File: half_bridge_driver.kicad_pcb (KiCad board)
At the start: 2 copper layers, 20 x 6 mm, 7 parts, among them J1 Conn_01x01_Male, J2 Conn_01x01_Male, U1 ZXGD3003E6, U2 ZXGD3003E6

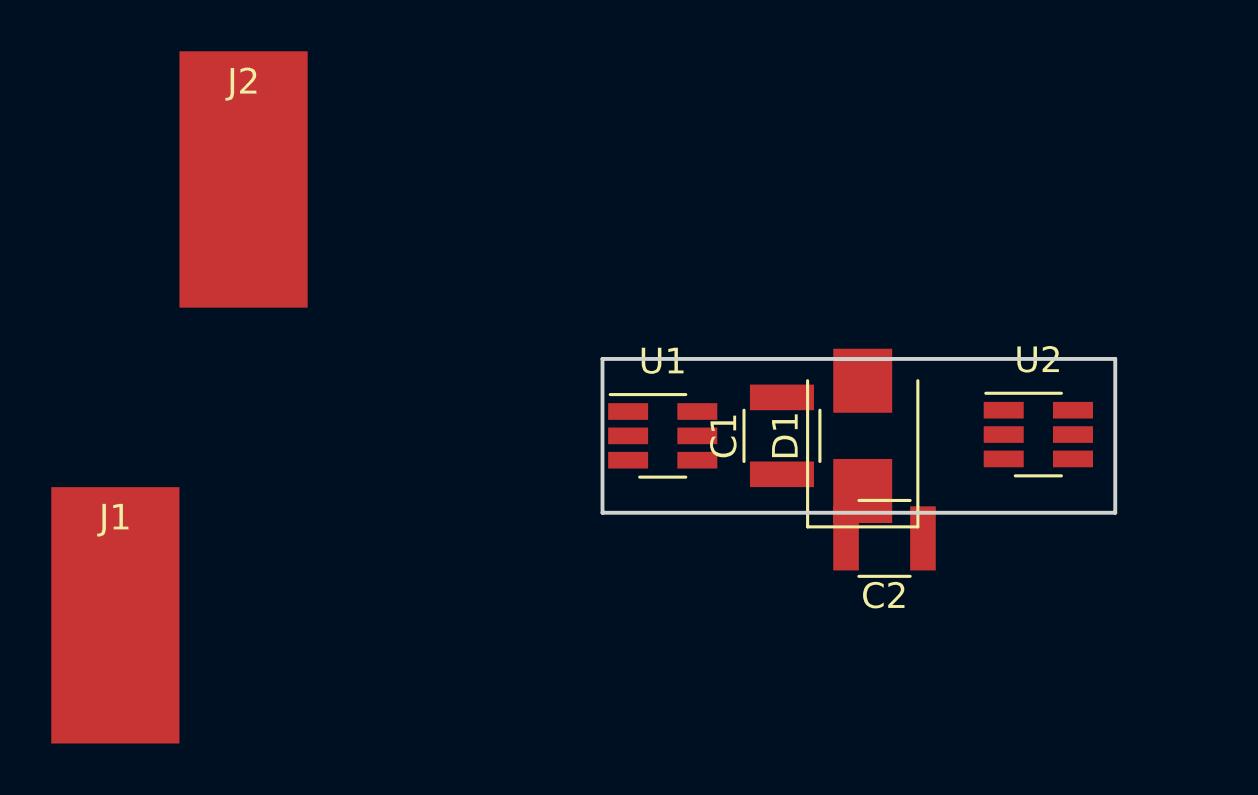
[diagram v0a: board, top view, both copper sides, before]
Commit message: Fixed high driver orientation and added one pad for external wiring.
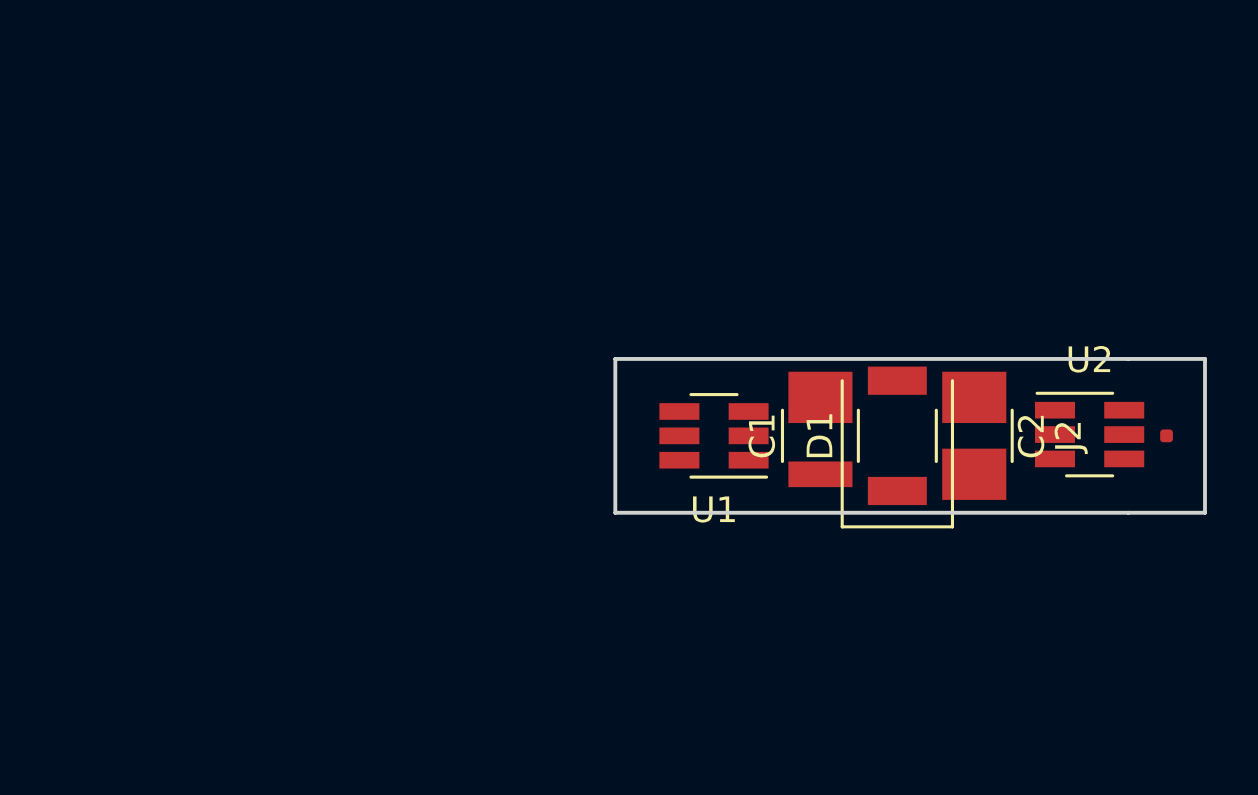
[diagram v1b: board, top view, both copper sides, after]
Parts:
- removed J1: Conn_01x01_Male, Wire_Pads:SolderWirePad_single_SMD_5x10mm
- C1, C2: value C -> 10µF
- D1: value D -> GB01SLT12-214
- moved J2 37.4 mm to (157.0, 90.0), turned to 90 degrees
- moved C2 5.32 mm to (149.5, 90.0), turned to 270 degrees
- moved U1 2.00 mm to (139.3, 90.0), turned to 180 degrees
- moved U2 2.00 mm to (154.0, 90.0)
- moved C1 1.50 mm to (143.5, 90.0)
- moved D1 1.35 mm to (146.5, 90.0)
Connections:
- U1 pad 1: /GND_High_Side -> /15V_High_Side
- U1 pad 3: /15V_High_Side -> /GND_High_Side
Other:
- board size 20 x 6 mm -> 23 x 6 mm
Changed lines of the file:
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@@
   (general
     (thickness 1.6)
-    (drawings 4)
+    (drawings 6)
     (tracks 0)
     (zones 0)
-    (modules 7)
+    (modules 6)
     (nets 9)
   )
@@
     (mod_text_size 1 1)
     (mod_text_width 0.15)
-    (pad_size 1.524 1.524)
-    (pad_drill 0.762)
+    (pad_size 0.5 0.5)
+    (pad_drill 0)
     (pad_to_mask_clearance 0.2)
     (aux_axis_origin 0 0)
@@
   )
   (module Capacitors_SMD:C_1210 (layer F.Cu)
-    (at 142 90 90)
+    (at 143.5 90 90)
     (descr "Capacitor SMD 1210, reflow soldering, AVX (see smccp.pdf)")
     (tags "capacitor 1210")
@@
       (effects (font (size 1 1) (thickness 0.15)))
     )
-    (fp_text value C (at 0 2.5 90) (layer F.Fab)
+    (fp_text value 10µF (at 0 2.5 90) (layer F.Fab)
       (effects (font (size 1 1) (thickness 0.15)))
     )
@@
       (effects (font (size 1 1) (thickness 0.15)))
     )
-    (pad 2 smd rect (at 1.5 0 90) (size 1 2.5) (layers F.Cu F.Paste F.Mask)
+    (pad 2 smd rect (at 1.5 0 90) (size 2 2.5) (layers F.Cu F.Paste F.Mask)
       (net 1 /GND_High_Side))
     (pad 1 smd rect (at -1.5 0 90) (size 1 2.5) (layers F.Cu F.Paste F.Mask)
@@
   )
   (module Capacitors_SMD:C_1210 (layer F.Cu)
-    (at 146 94 180)
+    (at 149.5 90 270)
     (descr "Capacitor SMD 1210, reflow soldering, AVX (see smccp.pdf)")
     (tags "capacitor 1210")
     (attr smd)
-    (fp_text reference C2 (at 0 -2.25 180) (layer F.SilkS)
-      (effects (font (size 1 1) (thickness 0.15)))
-    )
-    (fp_text value C (at 0 2.5 180) (layer F.Fab)
-      (effects (font (size 1 1) (thickness 0.15)))
-    )
-    (fp_text user %R (at 0 -2.25 180) (layer F.Fab)
+    (fp_text reference C2 (at 0 -2.25 270) (layer F.SilkS)
+      (effects (font (size 1 1) (thickness 0.15)))
+    )
+    (fp_text value 10µF (at 0 2.5 270) (layer F.Fab)
+      (effects (font (size 1 1) (thickness 0.15)))
+    )
+    (fp_text user %R (at 0 -2.25 270) (layer F.Fab)
       (effects (font (size 1 1) (thickness 0.15)))
     )
@@
     (fp_line (start 2.25 1.5) (end 2.25 -1.5) (layer F.CrtYd) (width 0.05))
     (fp_line (start 2.25 1.5) (end -2.25 1.5) (layer F.CrtYd) (width 0.05))
-    (pad 1 smd rect (at -1.5 0 180) (size 1 2.5) (layers F.Cu F.Paste F.Mask)
+    (pad 1 smd rect (at -1.5 0 270) (size 2 2.5) (layers F.Cu F.Paste F.Mask)
       (net 3 +15V))
-    (pad 2 smd rect (at 1.5 0 180) (size 1 2.5) (layers F.Cu F.Paste F.Mask)
+    (pad 2 smd rect (at 1.5 0 270) (size 2 2.5) (layers F.Cu F.Paste F.Mask)
       (net 4 GND))
     (model Capacitors_SMD.3dshapes/C_1210.wrl
@@
   )
   (module Diodes_SMD:D_SMB (layer F.Cu)
-    (at 145.15 90 90)
+    (at 146.5 90 90)
     (descr "Diode SMB (DO-214AA)")
     (tags "Diode SMB (DO-214AA)")
@@
       (effects (font (size 1 1) (thickness 0.15)))
     )
-    (fp_text value D (at 0 3.1 90) (layer F.Fab)
+    (fp_text value GB01SLT12-214 (at 0 3.1 90) (layer F.Fab)
       (effects (font (size 1 1) (thickness 0.15)))
     )
@@
       (effects (font (size 1 1) (thickness 0.15)))
     )
-    (pad 2 smd rect (at 2.15 0 90) (size 2.5 2.3) (layers F.Cu F.Paste F.Mask)
+    (pad 2 smd rect (at 2.15 0 90) (size 1.1 2.3) (layers F.Cu F.Paste F.Mask)
       (net 3 +15V))
-    (pad 1 smd rect (at -2.15 0 90) (size 2.5 2.3) (layers F.Cu F.Paste F.Mask)
+    (pad 1 smd rect (at -2.15 0 90) (size 1.1 2.3) (layers F.Cu F.Paste F.Mask)
       (net 1 /GND_High_Side))
     (model ${KISYS3DMOD}/Diodes_SMD.3dshapes/D_SMB.wrl
@@
   )
   (module Wire_Pads:SolderWirePad_single_SMD_5x10mm (layer F.Cu)
-    (at 116 97)
+    (at 157 90 90)
     (descr "Wire Pad, Square, SMD Pad,  5mm x 10mm,")
     (tags "MesurementPoint Square SMDPad 5mmx10mm ")
     (attr smd)
-    (fp_text reference J1 (at 0 -3.81) (layer F.SilkS)
-      (effects (font (size 1 1) (thickness 0.15)))
-    )
-    (fp_text value Conn_01x01_Male (at 0 6.35) (layer F.Fab)
-      (effects (font (size 1 1) (thickness 0.15)))
-    )
-    (fp_line (start -2.75 -5.25) (end -2.75 5.25) (layer F.CrtYd) (width 0.05))
-    (fp_line (start -2.75 5.25) (end 2.75 5.25) (layer F.CrtYd) (width 0.05))
-    (fp_line (start 2.75 5.25) (end 2.75 -5.25) (layer F.CrtYd) (width 0.05))
-    (fp_line (start 2.75 -5.25) (end -2.75 -5.25) (layer F.CrtYd) (width 0.05))
-    (pad 1 smd rect (at 0 0) (size 5 10) (layers F.Cu F.Paste F.Mask)
-      (net 5 /High_Side_Input))
-  )
-  (module Wire_Pads:SolderWirePad_single_SMD_5x10mm (layer F.Cu)
-    (at 121 80)
-    (descr "Wire Pad, Square, SMD Pad,  5mm x 10mm,")
-    (tags "MesurementPoint Square SMDPad 5mmx10mm ")
-    (attr smd)
-    (fp_text reference J2 (at 0 -3.81) (layer F.SilkS)
-      (effects (font (size 1 1) (thickness 0.15)))
-    )
-    (fp_text value Conn_01x01_Male (at 0 6.35) (layer F.Fab)
+    (fp_text reference J2 (at 0 -3.81 90) (layer F.SilkS)
+      (effects (font (size 1 1) (thickness 0.15)))
+    )
+    (fp_text value Conn_01x01_Male (at 0 6.35 90) (layer F.Fab) hide
       (effects (font (size 1 1) (thickness 0.15)))
     )
@@
     (fp_line (start -2.75 5.25) (end 2.75 5.25) (layer F.CrtYd) (width 0.05))
     (fp_line (start -2.75 -5.25) (end -2.75 5.25) (layer F.CrtYd) (width 0.05))
-    (pad 1 smd rect (at 0 0) (size 5 10) (layers F.Cu F.Paste F.Mask)
-      (net 6 /Low_Side_Input))
+    (pad 1 smd roundrect (at 0 0 90) (size 0.5 0.5) (layers F.Cu F.Paste F.Mask) (roundrect_rratio 0.25)
+      (net 6 /Low_Side_Input) (zone_connect 0))
   )
   (module TO_SOT_Packages_SMD:SOT-23-6_Handsoldering (layer F.Cu)
-    (at 137.35 90)
+    (at 139.35 90 180)
     (descr "6-pin SOT-23 package, Handsoldering")
     (tags "SOT-23-6 Handsoldering")
     (attr smd)
-    (fp_text reference U1 (at 0 -2.9) (layer F.SilkS)
-      (effects (font (size 1 1) (thickness 0.15)))
-    )
-    (fp_text value ZXGD3003E6 (at 0 2.9) (layer F.Fab)
+    (fp_text reference U1 (at 0 -2.9 180) (layer F.SilkS)
+      (effects (font (size 1 1) (thickness 0.15)))
+    )
+    (fp_text value ZXGD3003E6 (at 0 2.9 180) (layer F.Fab) hide
       (effects (font (size 1 1) (thickness 0.15)))
     )
@@
     (fp_line (start 0.9 -1.61) (end -2.05 -1.61) (layer F.SilkS) (width 0.12))
     (fp_line (start -0.9 1.61) (end 0.9 1.61) (layer F.SilkS) (width 0.12))
-    (fp_text user %R (at 0 0 90) (layer F.Fab)
+    (fp_text user %R (at 0 0 180) (layer F.Fab)
       (effects (font (size 0.5 0.5) (thickness 0.075)))
     )
-    (pad 5 smd rect (at 1.35 0) (size 1.56 0.65) (layers F.Cu F.Paste F.Mask)
+    (pad 5 smd rect (at 1.35 0 180) (size 1.56 0.65) (layers F.Cu F.Paste F.Mask)
       (net 5 /High_Side_Input))
-    (pad 6 smd rect (at 1.35 -0.95) (size 1.56 0.65) (layers F.Cu F.Paste F.Mask)
+    (pad 6 smd rect (at 1.35 -0.95 180) (size 1.56 0.65) (layers F.Cu F.Paste F.Mask)
       (net 7 /High_Side_MOSFET_Gate))
-    (pad 4 smd rect (at 1.35 0.95) (size 1.56 0.65) (layers F.Cu F.Paste F.Mask)
+    (pad 4 smd rect (at 1.35 0.95 180) (size 1.56 0.65) (layers F.Cu F.Paste F.Mask)
       (net 7 /High_Side_MOSFET_Gate))
-    (pad 3 smd rect (at -1.35 0.95) (size 1.56 0.65) (layers F.Cu F.Paste F.Mask)
+    (pad 3 smd rect (at -1.35 0.95 180) (size 1.56 0.65) (layers F.Cu F.Paste F.Mask)
+      (net 1 /GND_High_Side))
+    (pad 2 smd rect (at -1.35 0 180) (size 1.56 0.65) (layers F.Cu F.Paste F.Mask)
+      (net 5 /High_Side_Input))
+    (pad 1 smd rect (at -1.35 -0.95 180) (size 1.56 0.65) (layers F.Cu F.Paste F.Mask)
       (net 2 /15V_High_Side))
-    (pad 2 smd rect (at -1.35 0) (size 1.56 0.65) (layers F.Cu F.Paste F.Mask)
-      (net 5 /High_Side_Input))
-    (pad 1 smd rect (at -1.35 -0.95) (size 1.56 0.65) (layers F.Cu F.Paste F.Mask)
-      (net 1 /GND_High_Side))
     (model ${KISYS3DMOD}/TO_SOT_Packages_SMD.3dshapes/SOT-23-6.wrl
       (at (xyz 0 0 0))
@@
   )
   (module TO_SOT_Packages_SMD:SOT-23-6_Handsoldering (layer F.Cu)
-    (at 152 89.95)
+    (at 154 89.95)
     (descr "6-pin SOT-23 package, Handsoldering")
     (tags "SOT-23-6 Handsoldering")
@@
     )
   )
-  (gr_line (start 135 93) (end 135 87) (layer Edge.Cuts) (width 0.15))
-  (gr_line (start 155 93) (end 135 93) (layer Edge.Cuts) (width 0.15))
-  (gr_line (start 155 87) (end 155 93) (layer Edge.Cuts) (width 0.15))
-  (gr_line (start 135 87) (end 155 87) (layer Edge.Cuts) (width 0.15))
+  (gr_line (start 158.5 93) (end 155.5 93) (layer Edge.Cuts) (width 0.15))
+  (gr_line (start 158.5 87) (end 158.5 93) (layer Edge.Cuts) (width 0.15))
+  (gr_line (start 155.5 87) (end 158.5 87) (layer Edge.Cuts) (width 0.15))
+  (gr_line (start 135.5 93) (end 135.5 87) (layer Edge.Cuts) (width 0.15))
+  (gr_line (start 155.5 93) (end 135.5 93) (layer Edge.Cuts) (width 0.15))
+  (gr_line (start 135.5 87) (end 155.5 87) (layer Edge.Cuts) (width 0.15))
 )

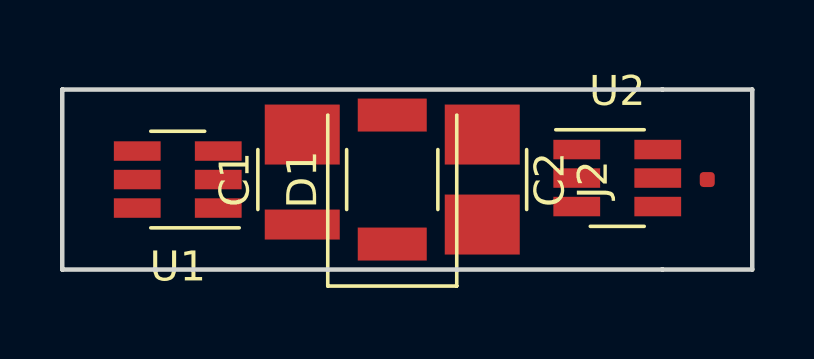
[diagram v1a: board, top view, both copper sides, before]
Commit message: Added extra pad to test external wiring.
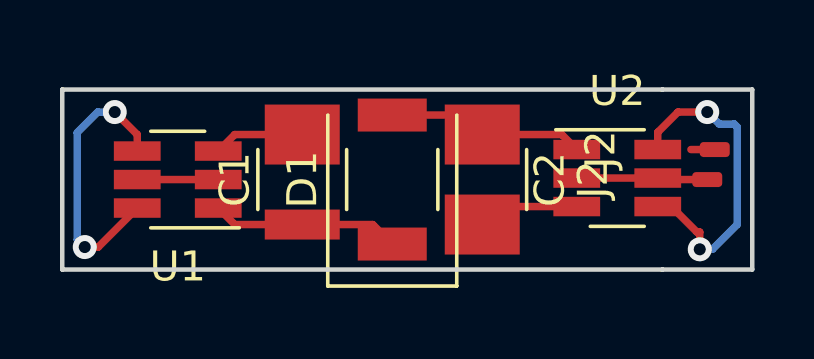
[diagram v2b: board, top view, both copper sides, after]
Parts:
- added J2: Conn_01x01_Male, Wire_Pads:SolderWirePad_single_SMD_5x10mm, F.Cu at (157.2, 89.0)
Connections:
- D1 pad 1: /GND_High_Side -> /15V_High_Side
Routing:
- net /Low_Side_MOSFET_Gate: track 0.00 -> 10.9 mm, vias 0 -> 2
- net /High_Side_MOSFET_Gate: track 0.00 -> 9.35 mm, vias 0 -> 2
- net +15V: track 0.00 -> 6.63 mm
- net /15V_High_Side: track 0.00 -> 6.30 mm
- net /Low_Side_Input: track 0.00 -> 4.37 mm
- net GND: track 0.00 -> 3.40 mm
- net /GND_High_Side: track 0.00 -> 3.03 mm
- net /High_Side_Input: track 0.00 -> 2.70 mm
- net (no net): track 0.00 -> 0.54 mm
- added copper zone on F.Cu, net GND
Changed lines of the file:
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@@
     (thickness 1.6)
     (drawings 6)
-    (tracks 0)
+    (tracks 42)
     (zones 0)
-    (modules 6)
+    (modules 7)
     (nets 9)
   )
@@
     (mod_text_size 1 1)
     (mod_text_width 0.15)
-    (pad_size 0.5 0.5)
+    (pad_size 0.5 1)
     (pad_drill 0)
     (pad_to_mask_clearance 0.2)
@@
     (add_net GND)
   )
+  (module Wire_Pads:SolderWirePad_single_SMD_5x10mm (layer F.Cu)
+    (at 157.25 89 90)
+    (descr "Wire Pad, Square, SMD Pad,  5mm x 10mm,")
+    (tags "MesurementPoint Square SMDPad 5mmx10mm ")
+    (attr smd)
+    (fp_text reference J2 (at 0 -3.81 90) (layer F.SilkS)
+      (effects (font (size 1 1) (thickness 0.15)))
+    )
+    (fp_text value Conn_01x01_Male (at 0 6.35 90) (layer F.Fab) hide
+      (effects (font (size 1 1) (thickness 0.15)))
+    )
+    (fp_line (start -2.75 -5.25) (end -2.75 5.25) (layer F.CrtYd) (width 0.05))
+    (fp_line (start -2.75 5.25) (end 2.75 5.25) (layer F.CrtYd) (width 0.05))
+    (fp_line (start 2.75 5.25) (end 2.75 -5.25) (layer F.CrtYd) (width 0.05))
+    (fp_line (start 2.75 -5.25) (end -2.75 -5.25) (layer F.CrtYd) (width 0.05))
+    (pad 1 smd roundrect (at 0 0 90) (size 0.5 1) (layers F.Cu F.Paste F.Mask) (roundrect_rratio 0.25)
+      (zone_connect 0))
+  )
   (module Capacitors_SMD:C_1210 (layer F.Cu)
     (at 143.5 90 90)
@@
       (net 3 +15V))
     (pad 1 smd rect (at -2.15 0 90) (size 1.1 2.3) (layers F.Cu F.Paste F.Mask)
-      (net 1 /GND_High_Side))
+      (net 2 /15V_High_Side))
     (model ${KISYS3DMOD}/Diodes_SMD.3dshapes/D_SMB.wrl
       (at (xyz 0 0 0))
@@
     (fp_line (start -2.75 5.25) (end 2.75 5.25) (layer F.CrtYd) (width 0.05))
     (fp_line (start -2.75 -5.25) (end -2.75 5.25) (layer F.CrtYd) (width 0.05))
-    (pad 1 smd roundrect (at 0 0 90) (size 0.5 0.5) (layers F.Cu F.Paste F.Mask) (roundrect_rratio 0.25)
+    (pad 1 smd roundrect (at 0 0 90) (size 0.5 1) (layers F.Cu F.Paste F.Mask) (roundrect_rratio 0.25)
       (net 6 /Low_Side_Input) (zone_connect 0))
   )
@@
   (gr_line (start 155.5 93) (end 135.5 93) (layer Edge.Cuts) (width 0.15))
   (gr_line (start 135.5 87) (end 155.5 87) (layer Edge.Cuts) (width 0.15))
+  (segment (start 157 89) (end 156.455001 89) (width 0.25) (layer F.Cu) (net 0))
+  (segment (start 141.25 88.5) (end 140.7 89.05) (width 0.25) (layer F.Cu) (net 1))
+  (segment (start 143.5 88.5) (end 141.25 88.5) (width 0.25) (layer F.Cu) (net 1))
+  (segment (start 145.85 91.5) (end 146.5 92.15) (width 0.25) (layer F.Cu) (net 2))
+  (segment (start 143.5 91.5) (end 145.85 91.5) (width 0.25) (layer F.Cu) (net 2))
+  (segment (start 141.25 91.5) (end 140.7 90.95) (width 0.25) (layer F.Cu) (net 2))
+  (segment (start 143.5 91.5) (end 141.25 91.5) (width 0.25) (layer F.Cu) (net 2))
+  (segment (start 148.85 87.85) (end 149.5 88.5) (width 0.25) (layer F.Cu) (net 3))
+  (segment (start 146.5 87.85) (end 148.85 87.85) (width 0.25) (layer F.Cu) (net 3))
+  (segment (start 152.15 88.5) (end 152.65 89) (width 0.25) (layer F.Cu) (net 3))
+  (segment (start 149.5 88.5) (end 152.15 88.5) (width 0.25) (layer F.Cu) (net 3))
+  (segment (start 150.1 90.9) (end 149.5 91.5) (width 0.25) (layer F.Cu) (net 4))
+  (segment (start 152.65 90.9) (end 150.1 90.9) (width 0.25) (layer F.Cu) (net 4))
+  (segment (start 140.7 90) (end 138 90) (width 0.25) (layer F.Cu) (net 5))
+  (segment (start 155.35 89.95) (end 152.65 89.95) (width 0.25) (layer F.Cu) (net 6))
+  (segment (start 155.4 90) (end 155.35 89.95) (width 0.25) (layer F.Cu) (net 6))
+  (segment (start 157 90) (end 155.4 90) (width 0.25) (layer F.Cu) (net 6))
+  (via (at 137.25 87.75) (size 0.8) (drill 0.4) (layers F.Cu B.Cu) (net 7))
+  (segment (start 138 89.05) (end 138 88.5) (width 0.25) (layer F.Cu) (net 7))
+  (segment (start 138 88.5) (end 137.25 87.75) (width 0.25) (layer F.Cu) (net 7))
+  (segment (start 136.684315 87.75) (end 136 88.434315) (width 0.25) (layer B.Cu) (net 7))
+  (segment (start 137.25 87.75) (end 136.684315 87.75) (width 0.25) (layer B.Cu) (net 7))
+  (via (at 136.25 92.25) (size 0.8) (drill 0.4) (layers F.Cu B.Cu) (net 7))
+  (segment (start 136 88.434315) (end 136 92) (width 0.25) (layer B.Cu) (net 7))
+  (segment (start 136 92) (end 136.25 92.25) (width 0.25) (layer B.Cu) (net 7))
+  (segment (start 136.7 92.25) (end 138 90.95) (width 0.25) (layer F.Cu) (net 7))
+  (segment (start 136.25 92.25) (end 136.7 92.25) (width 0.25) (layer F.Cu) (net 7))
+  (segment (start 155.35 88.425) (end 156.025 87.75) (width 0.25) (layer F.Cu) (net 8))
+  (segment (start 155.35 89) (end 155.35 88.425) (width 0.25) (layer F.Cu) (net 8))
+  (via (at 157 87.75) (size 0.8) (drill 0.4) (layers F.Cu B.Cu) (net 8))
+  (segment (start 156.025 87.75) (end 157 87.75) (width 0.25) (layer F.Cu) (net 8))
+  (segment (start 157.399999 88.149999) (end 157.899999 88.149999) (width 0.25) (layer B.Cu) (net 8))
+  (segment (start 157 87.75) (end 157.399999 88.149999) (width 0.25) (layer B.Cu) (net 8))
+  (segment (start 157.899999 88.149999) (end 158 88.25) (width 0.25) (layer B.Cu) (net 8))
+  (segment (start 158 88.25) (end 158 91.5) (width 0.25) (layer B.Cu) (net 8))
+  (via (at 156.75 92.325) (size 0.8) (drill 0.4) (layers F.Cu B.Cu) (net 8))
+  (segment (start 158 91.5) (end 157.175 92.325) (width 0.25) (layer B.Cu) (net 8))
+  (segment (start 157.175 92.325) (end 156.75 92.325) (width 0.25) (layer B.Cu) (net 8))
+  (segment (start 156.75 92.325) (end 156.75 91.75) (width 0.25) (layer F.Cu) (net 8))
+  (segment (start 155.805 90.9) (end 155.35 90.9) (width 0.25) (layer F.Cu) (net 8))
+  (segment (start 156.655 91.75) (end 155.805 90.9) (width 0.25) (layer F.Cu) (net 8))
+  (segment (start 156.75 91.75) (end 156.655 91.75) (width 0.25) (layer F.Cu) (net 8))
+  (zone (net 4) (net_name GND) (layer F.Cu) (hatch edge 0.508)
+    (connect_pads (clearance 0.508))
+    (min_thickness 0.254)
+    (fill yes (arc_segments 16) (thermal_gap 0.508) (thermal_bridge_width 0.508))
+    (polygon
+      (pts
+        (xy 158.5 87) (xy 135.5 87) (xy 135.5 93) (xy 158.5 93)
+      )
+    )
+  )
 )
